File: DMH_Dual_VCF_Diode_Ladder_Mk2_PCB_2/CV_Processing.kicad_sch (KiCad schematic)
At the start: 46 parts, among them J15 Conn_01x08_PinHeader, J16 Conn_01x08_PinHeader, SW10 SW_DPDT_OnOn, SW7 SW_SPDT_OnOffOn, SW9 SW_SPDT_OnOffOn, U7 TL074, U8 TL074

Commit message: Complete Exclude From Board on PCB 2
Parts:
- J15, J16: footprint Connector_PinHeader_2.54mm:PinHeader_1x08_P2.54mm_Vertical -> Connector_PinSocket_2.54mm:PinSocket_1x08_P2.54mm_Vertical
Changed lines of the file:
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@@
 			)
 		)
-		(property "Footprint" "Connector_PinHeader_2.54mm:PinHeader_1x08_P2.54mm_Vertical"
+		(property "Footprint" "Connector_PinSocket_2.54mm:PinSocket_1x08_P2.54mm_Vertical"
 			(at 69.85 106.68 0)
 			(effects
@@
 			)
 		)
-		(property "Footprint" "Connector_PinHeader_2.54mm:PinHeader_1x08_P2.54mm_Vertical"
+		(property "Footprint" "Connector_PinSocket_2.54mm:PinSocket_1x08_P2.54mm_Vertical"
 			(at 63.5 81.28 0)
 			(effects
@@
 			)
 		)
-		(property "Footprint" "Connector_PinHeader_2.54mm:PinHeader_1x08_P2.54mm_Vertical"
+		(property "Footprint" "Connector_PinSocket_2.54mm:PinSocket_1x08_P2.54mm_Vertical"
 			(at 119.38 38.1 0)
 			(effects
@@
 			)
 		)
-		(property "Footprint" "Connector_PinHeader_2.54mm:PinHeader_1x08_P2.54mm_Vertical"
+		(property "Footprint" "Connector_PinSocket_2.54mm:PinSocket_1x08_P2.54mm_Vertical"
 			(at 160.02 101.6 0)
 			(effects
@@
 			)
 		)
-		(property "Footprint" "Connector_PinHeader_2.54mm:PinHeader_1x08_P2.54mm_Vertical"
+		(property "Footprint" "Connector_PinSocket_2.54mm:PinSocket_1x08_P2.54mm_Vertical"
 			(at 140.97 101.6 0)
 			(effects
@@
 			)
 		)
-		(property "Footprint" "Connector_PinHeader_2.54mm:PinHeader_1x08_P2.54mm_Vertical"
+		(property "Footprint" "Connector_PinSocket_2.54mm:PinSocket_1x08_P2.54mm_Vertical"
 			(at 52.07 201.93 0)
 			(effects
@@
 			)
 		)
-		(property "Footprint" "Connector_PinHeader_2.54mm:PinHeader_1x08_P2.54mm_Vertical"
+		(property "Footprint" "Connector_PinSocket_2.54mm:PinSocket_1x08_P2.54mm_Vertical"
 			(at 127 170.18 0)
 			(effects
@@
 			)
 		)
-		(property "Footprint" "Connector_PinHeader_2.54mm:PinHeader_1x08_P2.54mm_Vertical"
+		(property "Footprint" "Connector_PinSocket_2.54mm:PinSocket_1x08_P2.54mm_Vertical"
 			(at 38.1 182.88 0)
 			(effects
@@
 			)
 		)
-		(property "Footprint" "Connector_PinHeader_2.54mm:PinHeader_1x08_P2.54mm_Vertical"
+		(property "Footprint" "Connector_PinSocket_2.54mm:PinSocket_1x08_P2.54mm_Vertical"
 			(at 77.47 227.33 0)
 			(effects
@@
 			)
 		)
-		(property "Footprint" "Connector_PinHeader_2.54mm:PinHeader_1x08_P2.54mm_Vertical"
+		(property "Footprint" "Connector_PinSocket_2.54mm:PinSocket_1x08_P2.54mm_Vertical"
 			(at 77.47 100.33 0)
 			(effects
@@
 			)
 		)
-		(property "Footprint" "Connector_PinHeader_2.54mm:PinHeader_1x08_P2.54mm_Vertical"
+		(property "Footprint" "Connector_PinSocket_2.54mm:PinSocket_1x08_P2.54mm_Vertical"
 			(at 63.5 208.28 0)
 			(effects
@@
 			)
 		)
-		(property "Footprint" "Connector_PinHeader_2.54mm:PinHeader_1x08_P2.54mm_Vertical"
+		(property "Footprint" "Connector_PinSocket_2.54mm:PinSocket_1x08_P2.54mm_Vertical"
 			(at 140.97 177.8 0)
 			(effects
@@
 			)
 		)
-		(property "Footprint" "Connector_PinHeader_2.54mm:PinHeader_1x08_P2.54mm_Vertical"
+		(property "Footprint" "Connector_PinSocket_2.54mm:PinSocket_1x08_P2.54mm_Vertical"
 			(at 171.45 134.62 0)
 			(effects
@@
 			)
 		)
-		(property "Footprint" "Connector_PinHeader_2.54mm:PinHeader_1x08_P2.54mm_Vertical"
+		(property "Footprint" "Connector_PinSocket_2.54mm:PinSocket_1x08_P2.54mm_Vertical"
 			(at 38.1 55.88 0)
 			(effects
@@
 			)
 		)
-		(property "Footprint" "Connector_PinHeader_2.54mm:PinHeader_1x08_P2.54mm_Vertical"
+		(property "Footprint" "Connector_PinSocket_2.54mm:PinSocket_1x08_P2.54mm_Vertical"
 			(at 52.07 74.93 0)
 			(effects
@@
 			)
 		)
-		(property "Footprint" "Connector_PinHeader_2.54mm:PinHeader_1x08_P2.54mm_Vertical"
+		(property "Footprint" "Connector_PinSocket_2.54mm:PinSocket_1x08_P2.54mm_Vertical"
 			(at 69.85 233.68 0)
 			(effects

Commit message: pcb 2 routing in progress
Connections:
- net CV A: now also J15.5 (Pin_5); no longer J15.7 (Pin_7)
- net CV B: now also J16.5 (Pin_5); no longer J16.7 (Pin_7)
- net CV1 A Input: now also J15.3 (Pin_3); no longer J15.2 (Pin_2)
- net CV1 B Input: now also J16.4 (Pin_4); no longer J16.2 (Pin_2)
- net CV2 A Input: now also J15.6 (Pin_6); no longer J15.4 (Pin_4)
- net CV2 B Input: now also J16.8 (Pin_8); no longer J16.4 (Pin_4)
- net CV3 A Input: now also J15.2 (Pin_2); no longer J15.6 (Pin_6)
- net CV3 B Input: now also J16.2 (Pin_2); no longer J16.6 (Pin_6)
- net Link CV Switch: now also J16.6 (Pin_6); no longer J16.8 (Pin_8)
- net at RV11.2, U8.5 (+): now also J16.7 (Pin_7); no longer J16.5 (Pin_5)
- net at RV3.2, U7.12 (+): now also J15.4 (Pin_4); no longer J15.3 (Pin_3)
- net at RV5.2, U7.10 (+): now also J15.7 (Pin_7); no longer J15.5 (Pin_5)
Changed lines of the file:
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@@
 		(lib_id "SynthStuff:Conn_01x08_PinHeader")
 		(at 69.85 106.68 270)
-		(unit 6)
+		(unit 2)
 		(exclude_from_sim no)
 		(in_bom yes)
@@
 				(path "/58f4306d-5387-4983-bb08-41a2313fd315/ec2d44bc-ed06-4f0b-a22e-df640fa5e089"
 					(reference "J15")
-					(unit 6)
+					(unit 2)
 				)
 			)
@@
 		(lib_id "SynthStuff:Conn_01x08_PinHeader")
 		(at 63.5 81.28 270)
-		(unit 4)
+		(unit 6)
 		(exclude_from_sim no)
 		(in_bom yes)
@@
 				(path "/58f4306d-5387-4983-bb08-41a2313fd315/ec2d44bc-ed06-4f0b-a22e-df640fa5e089"
 					(reference "J15")
-					(unit 4)
+					(unit 6)
 				)
 			)
@@
 		(lib_id "SynthStuff:Conn_01x08_PinHeader")
 		(at 140.97 101.6 0)
-		(unit 7)
+		(unit 5)
 		(exclude_from_sim no)
 		(in_bom yes)
@@
 				(path "/58f4306d-5387-4983-bb08-41a2313fd315/ec2d44bc-ed06-4f0b-a22e-df640fa5e089"
 					(reference "J15")
-					(unit 7)
+					(unit 5)
 				)
 			)
@@
 		(at 38.1 182.88 90)
 		(mirror x)
-		(unit 2)
+		(unit 4)
 		(exclude_from_sim no)
 		(in_bom yes)
@@
 				(path "/58f4306d-5387-4983-bb08-41a2313fd315/ec2d44bc-ed06-4f0b-a22e-df640fa5e089"
 					(reference "J16")
-					(unit 2)
+					(unit 4)
 				)
 			)
@@
 		(lib_id "SynthStuff:Conn_01x08_PinHeader")
 		(at 77.47 227.33 90)
-		(unit 5)
+		(unit 7)
 		(exclude_from_sim no)
 		(in_bom yes)
@@
 				(path "/58f4306d-5387-4983-bb08-41a2313fd315/ec2d44bc-ed06-4f0b-a22e-df640fa5e089"
 					(reference "J16")
-					(unit 5)
+					(unit 7)
 				)
 			)
@@
 		(at 77.47 100.33 270)
 		(mirror x)
-		(unit 5)
+		(unit 7)
 		(exclude_from_sim no)
 		(in_bom yes)
@@
 				(path "/58f4306d-5387-4983-bb08-41a2313fd315/ec2d44bc-ed06-4f0b-a22e-df640fa5e089"
 					(reference "J15")
-					(unit 5)
+					(unit 7)
 				)
 			)
@@
 		(at 63.5 208.28 90)
 		(mirror x)
-		(unit 4)
+		(unit 8)
 		(exclude_from_sim no)
 		(in_bom yes)
@@
 				(path "/58f4306d-5387-4983-bb08-41a2313fd315/ec2d44bc-ed06-4f0b-a22e-df640fa5e089"
 					(reference "J16")
-					(unit 4)
+					(unit 8)
 				)
 			)
@@
 		(lib_id "SynthStuff:Conn_01x08_PinHeader")
 		(at 140.97 177.8 0)
-		(unit 7)
+		(unit 5)
 		(exclude_from_sim no)
 		(in_bom yes)
@@
 				(path "/58f4306d-5387-4983-bb08-41a2313fd315/ec2d44bc-ed06-4f0b-a22e-df640fa5e089"
 					(reference "J16")
-					(unit 7)
+					(unit 5)
 				)
 			)
@@
 		(lib_id "SynthStuff:Conn_01x08_PinHeader")
 		(at 171.45 134.62 270)
-		(unit 8)
+		(unit 6)
 		(exclude_from_sim no)
 		(in_bom yes)
@@
 				(path "/58f4306d-5387-4983-bb08-41a2313fd315/ec2d44bc-ed06-4f0b-a22e-df640fa5e089"
 					(reference "J16")
-					(unit 8)
+					(unit 6)
 				)
 			)
@@
 		(at 38.1 55.88 90)
 		(mirror x)
-		(unit 2)
+		(unit 3)
 		(exclude_from_sim no)
 		(in_bom yes)
@@
 				(path "/58f4306d-5387-4983-bb08-41a2313fd315/ec2d44bc-ed06-4f0b-a22e-df640fa5e089"
 					(reference "J15")
-					(unit 2)
+					(unit 3)
 				)
 			)
@@
 		(lib_id "SynthStuff:Conn_01x08_PinHeader")
 		(at 52.07 74.93 90)
-		(unit 3)
+		(unit 4)
 		(exclude_from_sim no)
 		(in_bom yes)
@@
 				(path "/58f4306d-5387-4983-bb08-41a2313fd315/ec2d44bc-ed06-4f0b-a22e-df640fa5e089"
 					(reference "J15")
-					(unit 3)
+					(unit 4)
 				)
 			)
@@
 		(lib_id "SynthStuff:Conn_01x08_PinHeader")
 		(at 69.85 233.68 270)
-		(unit 6)
+		(unit 2)
 		(exclude_from_sim no)
 		(in_bom yes)
@@
 				(path "/58f4306d-5387-4983-bb08-41a2313fd315/ec2d44bc-ed06-4f0b-a22e-df640fa5e089"
 					(reference "J16")
-					(unit 6)
+					(unit 2)
 				)
 			)

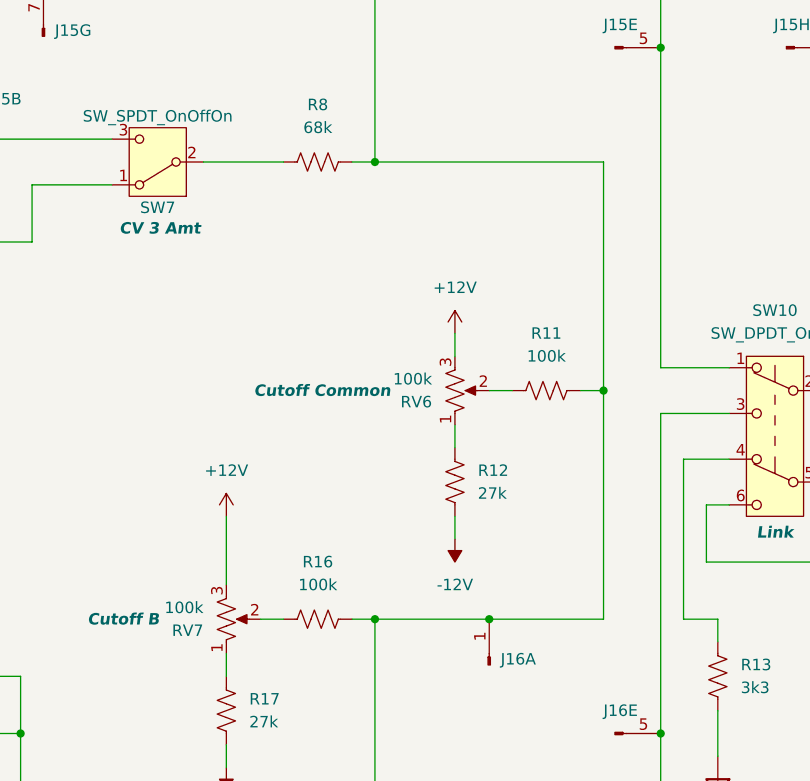
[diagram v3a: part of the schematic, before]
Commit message: Replaced Central Cutoff pot with dual port
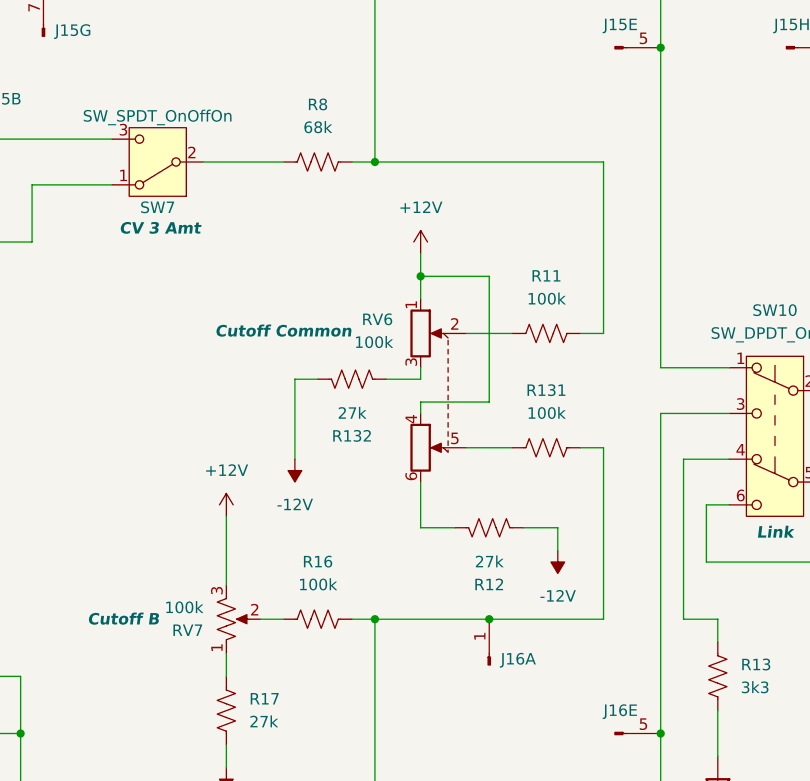
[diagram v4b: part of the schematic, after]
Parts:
- removed RV6: 100k, SynthStuff:Potentiometer_Alpha_RD901F-40-00D_Single_Vertical, symbol Device:R_Potentiometer_US
- added R131: 100k, Resistor_THT:R_Axial_DIN0207_L6.3mm_D2.5mm_P7.62mm_Horizontal, symbol Device:R_US
- added R132: 27k, Resistor_THT:R_Axial_DIN0207_L6.3mm_D2.5mm_P7.62mm_Horizontal, symbol Device:R_US
- added RV6: 100k, Potentiometer_THT:Potentiometer_Alpha_RD902F-40-00D_Dual_Vertical, symbol Device:R_Potentiometer_Dual
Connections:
- net +12V: now also RV6.1, RV6.4
- net -12V: now also R132.2
- net at J15.1 (Pin_1), R1.2, R11.2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: no longer J16.1 (Pin_1), R16.2, R19.2, R20.1, R22.2, R23.1, U8.13 (-)
- net at R12.1: now also RV6.6
- net at R11.1: now also RV6.2
- new net: J16.1 (Pin_1), R131.2, R16.2, R19.2, R20.1, R22.2, R23.1, U8.13 (-)
- new net: R132.1, RV6.3
- new net: R131.1, RV6.5
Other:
- moved on the sheet: R11, R12

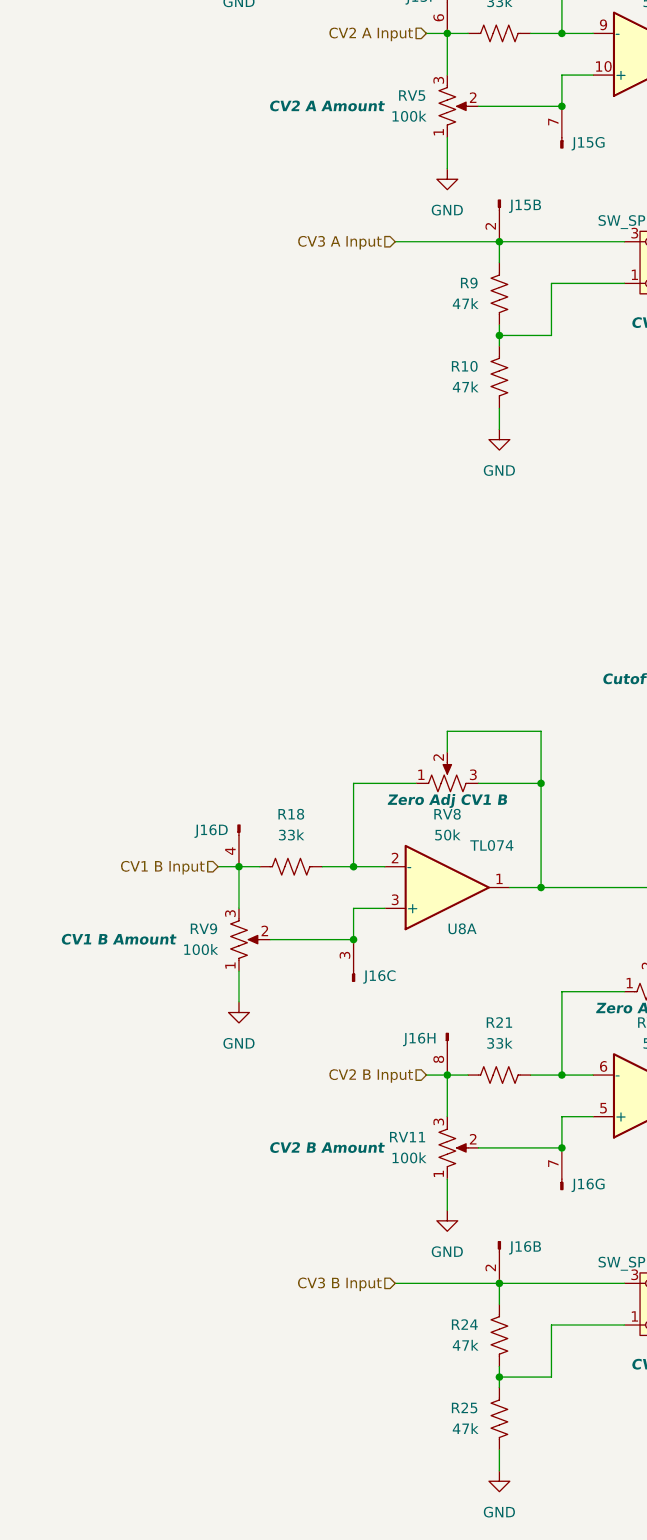
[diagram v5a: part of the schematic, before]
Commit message: Added buffering to each CV 3 input separately
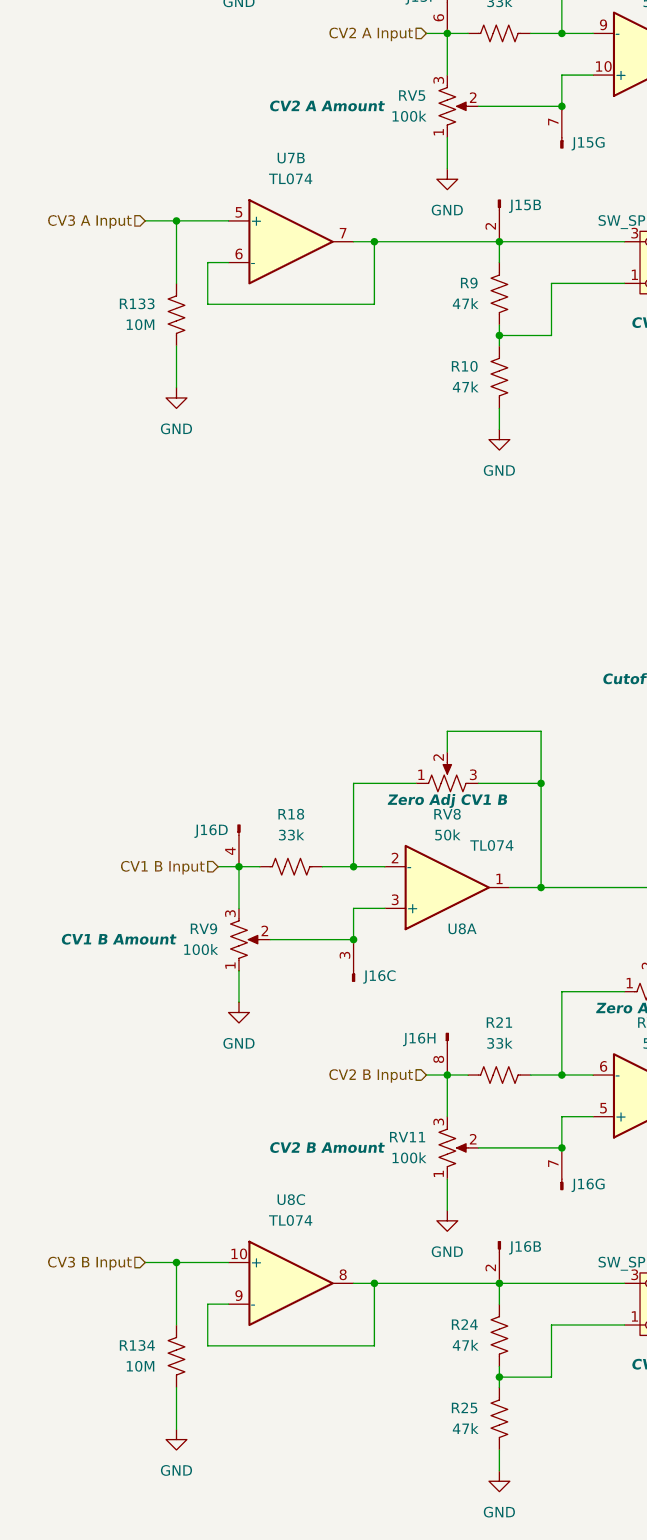
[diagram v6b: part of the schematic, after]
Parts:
- added R133, R134: 10M, Resistor_THT:R_Axial_DIN0207_L6.3mm_D2.5mm_P7.62mm_Horizontal, symbol Device:R_US
- added unit 2 of U7
- added unit 3 of U8
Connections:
- net CV3 A Input: now also R133.2, U7.5 (+); no longer J15.2 (Pin_2), R9.2, SW7.3 (C)
- net CV3 B Input: now also R134.2, U8.10 (+); no longer J16.2 (Pin_2), R24.2, SW9.3 (C)
- net GND: now also R133.1, R134.1
- new net: J15.2 (Pin_2), R9.2, SW7.3 (C), U7.6 (-), U7.7
- new net: J16.2 (Pin_2), R24.2, SW9.3 (C), U8.8, U8.9 (-)
